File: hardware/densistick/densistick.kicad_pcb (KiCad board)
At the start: 4 copper layers, 85 x 22 mm, 60 parts, among them J1 Cable, SW1 SW_Push, U1 TSL2585, U2 USBLC6-2SC6, U3 MIC4812, U4 FT260Q, U5 MIC5365-1.8YC5, U6 CAT24C08, U7 MCP4017-104E/LT

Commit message: Add initial panelization and automation bits
This brings in some KiKit infrastructure bits (tab markers, JSON config
files, support scripts) and a Makefile to run it all.

The actual panelization approach for the various boards in this project
is still TBD, pending conversation with assembly houses. However, this
puts in place some basic things to support it.

Ref #59
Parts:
- added REF**: Tab, PCM_kikit:Tab, F.Cu at (126.5, 68.0)
- added REF**: Tab, PCM_kikit:Tab, F.Cu at (40.5, 68.0)
- added REF**: Tab, PCM_kikit:Tab, F.Cu at (67.0, 56.5)
- added REF**: Tab, PCM_kikit:Tab, F.Cu at (106.0, 79.5)
- added REF**: Tab, PCM_kikit:Tab, F.Cu at (106.0, 56.5)
- added REF**: Tab, PCM_kikit:Tab, F.Cu at (67.0, 79.5)

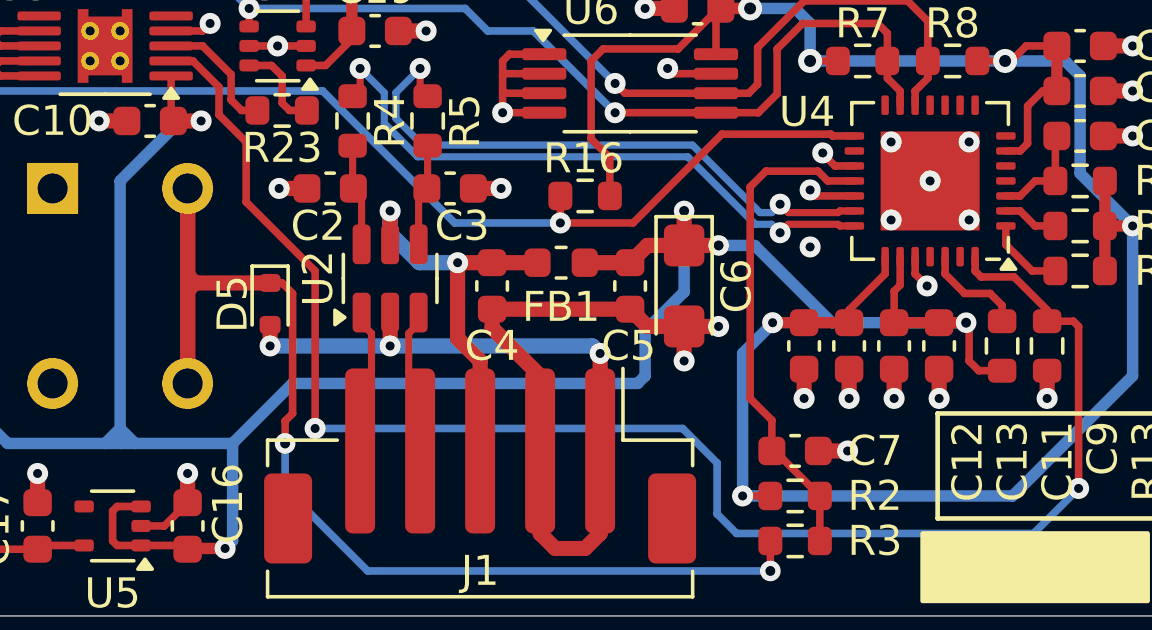
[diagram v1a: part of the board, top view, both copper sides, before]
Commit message: Various bits of TVS and layout cleanup for the meter probe and DensiStick
Decided to standardize on the new TI ESD321 TVS diode for single-line
protection on these boards. This part appears designed for this use,
especially with a lower working voltage. Its also in a similar package
to the Semtech part previously being used in some of these cases.

Created a new SOD-523 footprint based on TI's recommended land pattern,
which might work a little better than the stock one.

Updated the DensiStick to use the same 4.7uF MLCC for the bulk input
capacitor as the meter probe.

Various other minor tweaks to the fab layers and traces associated with
the above changes.
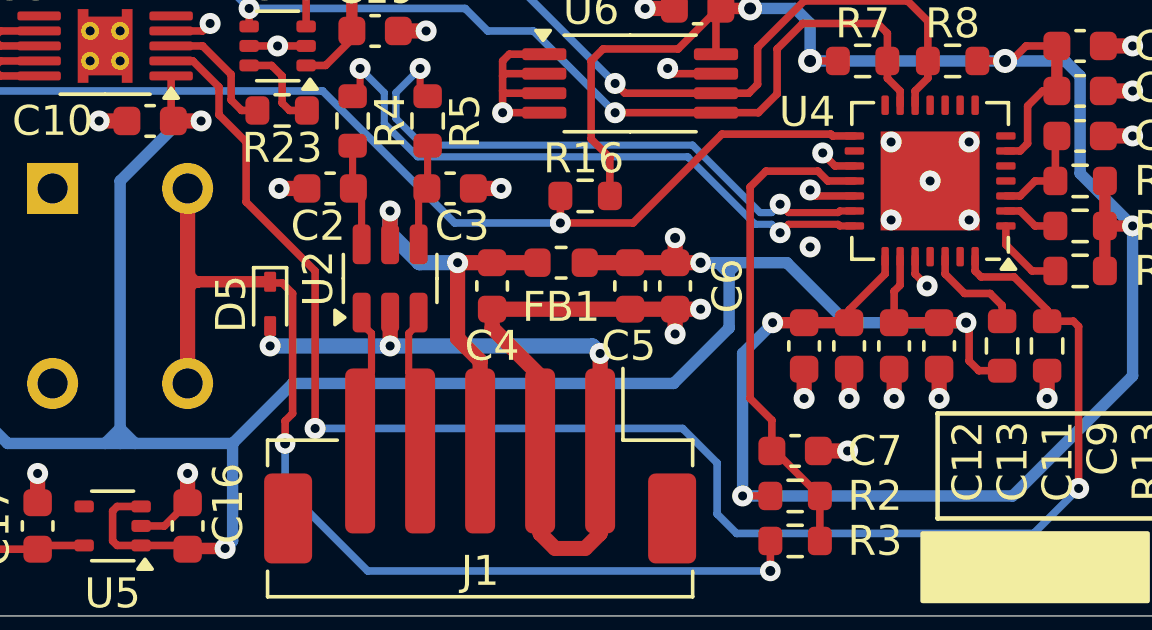
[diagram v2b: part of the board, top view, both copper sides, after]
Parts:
- C6: footprint Capacitor_Tantalum_SMD:CP_EIA-3216-18_Kemet-A -> Capacitor_SMD:C_0603_1608Metric
- D5: value uClamp0501H -> ESD321; footprint Diode_SMD:D_SOD-523 -> lib_fp:D_TI_SOD-523_DYA0002A
- FB1: value 600R@100MHz -> 600R
- moved C6 0.30 mm to (101.5, 68.0)
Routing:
- net Net-(D5-K): track 41.5 -> 36.0 mm
- net GND: track 52.1 -> 51.0 mm

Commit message: Minor paste clearance settings changes
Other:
- rule pad_to_mask_clearance: 0.05 -> 0
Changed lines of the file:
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@@
 			(dielectric_constraints yes)
 		)
-		(pad_to_mask_clearance 0.05)
+		(pad_to_mask_clearance 0)
+		(pad_to_paste_clearance -0.05)
 		(allow_soldermask_bridges_in_footprints no)
 		(aux_axis_origin 41 79)
@@
 		(tags "Diode SOD523 TI DYA0002A")
 		(property "Reference" "D5"
-			(at 0 1.3 -90)
+			(at 0 1.3 90)
 			(layer "F.SilkS")
 			(effects
@@
 		)
 		(property "Value" "ESD321"
-			(at 0 1 -90)
+			(at 0 1 90)
 			(layer "F.Fab")
 			(effects
@@
 		(sheetname "Root")
 		(sheetfile "densistick.kicad_sch")
+		(solder_paste_margin -0.025)
 		(attr smd)
 		(fp_line
@@
 		)
 		(fp_text user "${REFERENCE}"
-			(at 0 -1.3 -90)
+			(at 0 -1.3 90)
 			(layer "F.Fab")
 			(hide yes)
@@
 		(sheetname "Root")
 		(sheetfile "densistick.kicad_sch")
+		(solder_paste_margin -0.025)
 		(attr smd)
 		(fp_line
@@
 	)
 	(zone
-		(net 7)
-		(net_name "Net-(D5-K)")
+		(net 5)
+		(net_name "/RLED1")
 		(layer "F.Cu")
-		(name "$teardrop_padvia$")
-		(hatch full 0.1)
-		(priority 30000)
-		(attr
-			(teardrop
-				(type padvia)
-			)
-		)
+		(hatch edge 0.5)
+		(priority 6)
 		(connect_pads yes
-			(clearance 0)
+			(clearance 0.508)
 		)
-		(min_thickness 0.0254)
+		(min_thickness 0.25)
 		(filled_areas_thickness no)
 		(fill yes
 			(thermal_gap 0.5)
 			(thermal_bridge_width 0.5)
-			(island_removal_mode 1)
-			(island_area_min 10)
 		)
 		(polygon
 			(pts
-				(xy 85.504 69.55) (xy 84.996 69.55) (xy 84.464702 70.924719) (xy 85.25 71.251) (xy 86.035298 70.924719)
+				(xy 47 70) (xy 48 70) (xy 48 65) (xy 42 65) (xy 42 70) (xy 43 70) (xy 43 68.25) (xy 47 68.25)
 			)
 		)
 	)
 	(zone
-		(net 5)
-		(net_name "/RLED1")
+		(net 3)
+		(net_name "+5V")
 		(layer "F.Cu")
 		(hatch edge 0.5)
-		(priority 6)
+		(priority 7)
 		(connect_pads yes
 			(clearance 0.508)
@@
 		(polygon
 			(pts
-				(xy 47 70) (xy 48 70) (xy 48 65) (xy 42 65) (xy 42 70) (xy 43 70) (xy 43 68.25) (xy 47 68.25)
+				(xy 76.5 69.5) (xy 76.5 70.25) (xy 76.75 70.5) (xy 78 70.5) (xy 78 71.5) (xy 72 71.5) (xy 72 70.5)
+				(xy 73.25 70.5) (xy 73.5 70.25) (xy 73.5 69.5)
 			)
 		)
 	)
 	(zone
-		(net 3)
-		(net_name "+5V")
+		(net 7)
+		(net_name "Net-(D5-K)")
 		(layer "F.Cu")
-		(hatch edge 0.5)
-		(priority 7)
+		(name "$teardrop_padvia$")
+		(hatch full 0.1)
+		(priority 30001)
+		(attr
+			(teardrop
+				(type padvia)
+			)
+		)
 		(connect_pads yes
-			(clearance 0.508)
+			(clearance 0)
 		)
-		(min_thickness 0.25)
+		(min_thickness 0.0254)
 		(filled_areas_thickness no)
 		(fill yes
 			(thermal_gap 0.5)
 			(thermal_bridge_width 0.5)
+			(island_removal_mode 1)
+			(island_area_min 10)
 		)
 		(polygon
 			(pts
-				(xy 76.5 69.5) (xy 76.5 70.25) (xy 76.75 70.5) (xy 78 70.5) (xy 78 71.5) (xy 72 71.5) (xy 72 70.5)
-				(xy 73.25 70.5) (xy 73.5 70.25) (xy 73.5 69.5)
+				(xy 84.996 66.45) (xy 85.504 66.45) (xy 86.035298 65.075281) (xy 85.25 64.749) (xy 84.464702 65.075281)
 			)
 		)
@@
 		(name "$teardrop_padvia$")
 		(hatch full 0.1)
-		(priority 30001)
+		(priority 30000)
 		(attr
 			(teardrop
@@
 		(polygon
 			(pts
-				(xy 84.996 66.45) (xy 85.504 66.45) (xy 86.035298 65.075281) (xy 85.25 64.749) (xy 84.464702 65.075281)
+				(xy 85.504 69.55) (xy 84.996 69.55) (xy 84.464702 70.924719) (xy 85.25 71.251) (xy 86.035298 70.924719)
 			)
 		)
